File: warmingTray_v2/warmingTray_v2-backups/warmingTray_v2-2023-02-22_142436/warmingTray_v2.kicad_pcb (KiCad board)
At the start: 2 copper layers, 37 parts, among them J1 Jack-DC, P1 Power, P2 Analog, P3 Analog, P4 Digital, P5 PWM, P6 PWM, P7 Communication

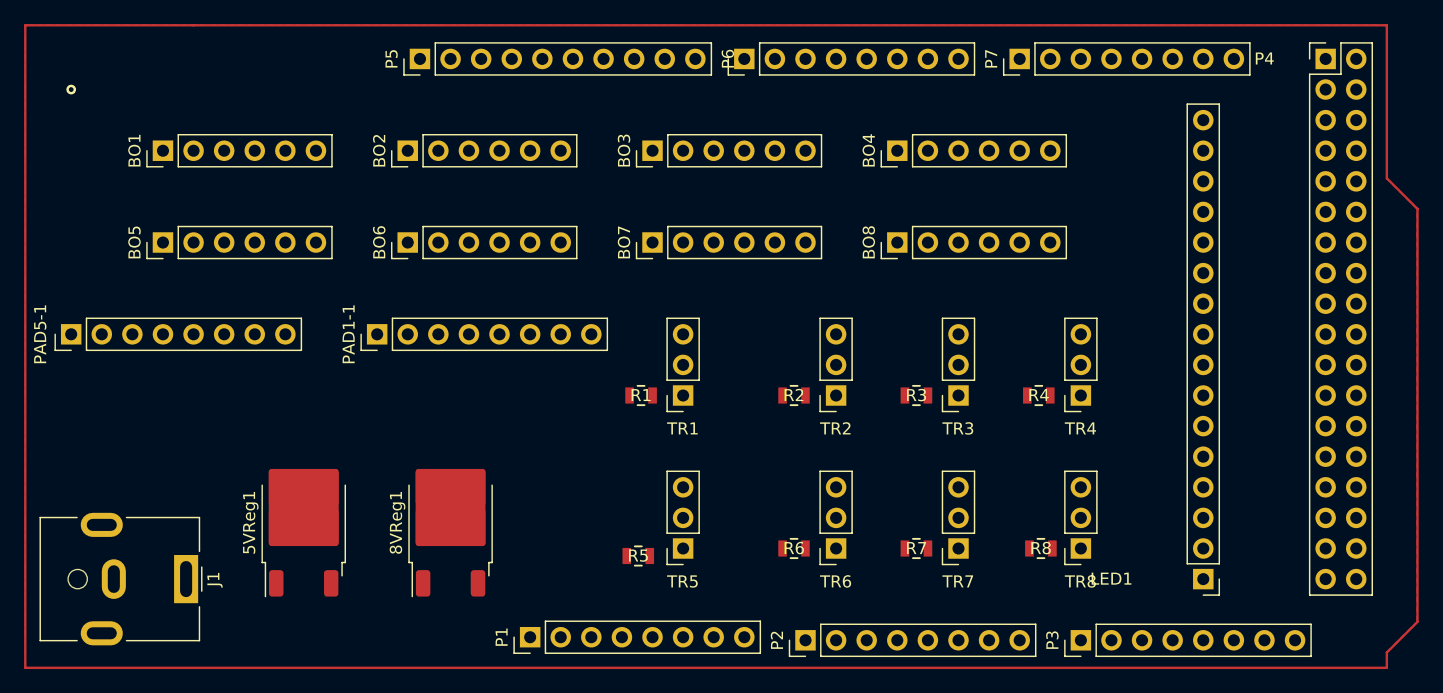
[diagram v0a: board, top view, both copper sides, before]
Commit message: Added footprints for transistor pins and surface mount resistors
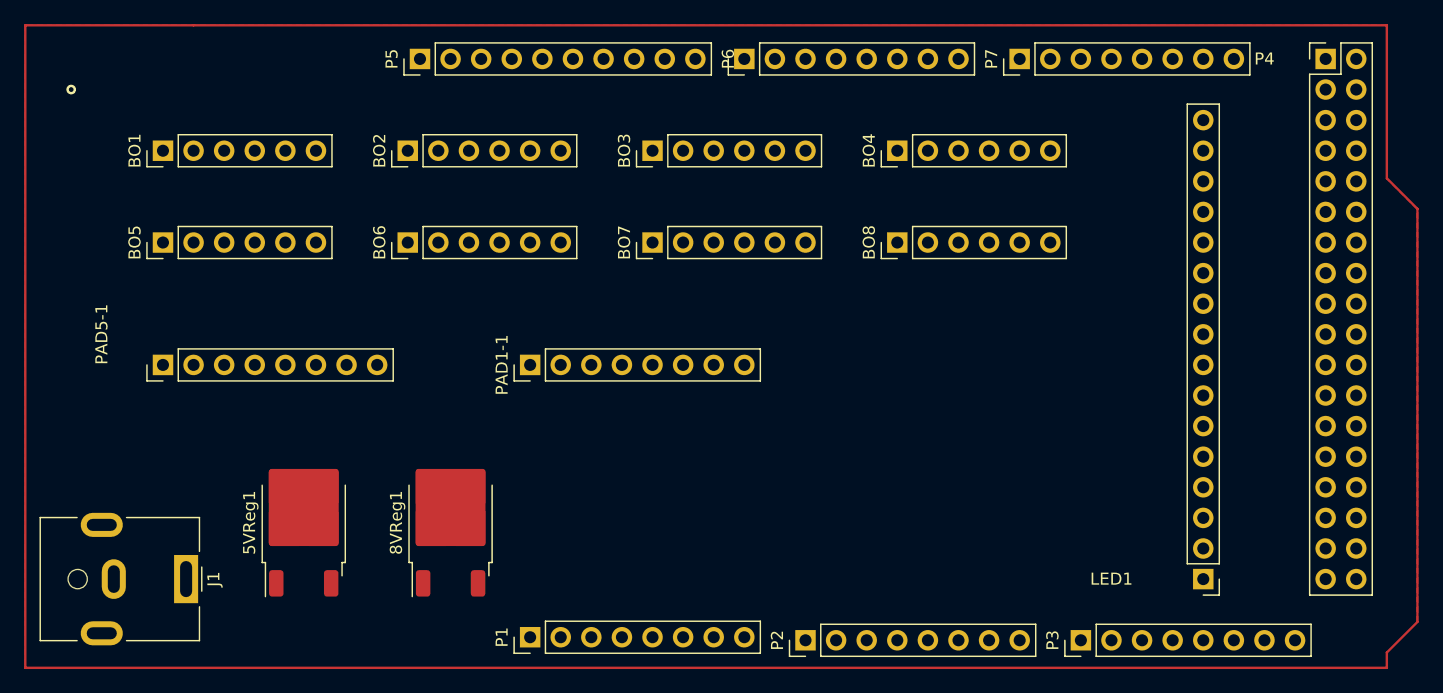
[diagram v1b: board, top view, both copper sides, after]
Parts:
- removed R1, R2, R3, R4, R5, R6, R7, R8: R, footprints:RES_RK73G2A_KOA
- removed TR1, TR2, TR3, TR4, TR5, TR6, TR7, TR8: Conn_01x03, Connector_PinSocket_2.54mm:PinSocket_1x03_P2.54mm_Vertical
- moved PAD1-1 13.0 mm to (142.2, 96.5)
- moved PAD5-1 8.03 mm to (111.8, 96.5)
